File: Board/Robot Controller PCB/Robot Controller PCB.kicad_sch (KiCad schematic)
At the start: 1 part

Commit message: Started shematic
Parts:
- added R, R?: 10k, symbol Device:R_Small_US
- added R?: 20k, symbol Device:R_Small_US
- added R?: 80k, symbol Device:R_Small_US
- added R?: 40k, symbol Device:R_Small_US
- added SW? (x2): SW_DPST_x2, symbol Switch:SW_DPST_x2
- added SW?: SW_DIP_x04, symbol Switch:SW_DIP_x04
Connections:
- net +5V: now reaches U?.21 (VCC)
- net +5V: now also SW?.1, SW?.2, SW?.3, SW?.4
- net GND: now reaches U?.23 (GND)
- net GND: now also U?.3 (GND), U?.4 (GND), R?.2, SW?.1 (A), SW?.3 (A)
- net at U?.5 (D2): now also SW?.2 (B)
- net at U?.6 (~D3): now also SW?.4 (B)
- net at U?.7 (D4/A6): now also R.1, R?.1, R?.2, R?.2, R?.2
- new net: R?.1, SW?.7
- new net: R?.1, SW?.5
- new net: R.2, SW?.8
- new net: R?.1, SW?.6
- no-connect marks 0 -> 5

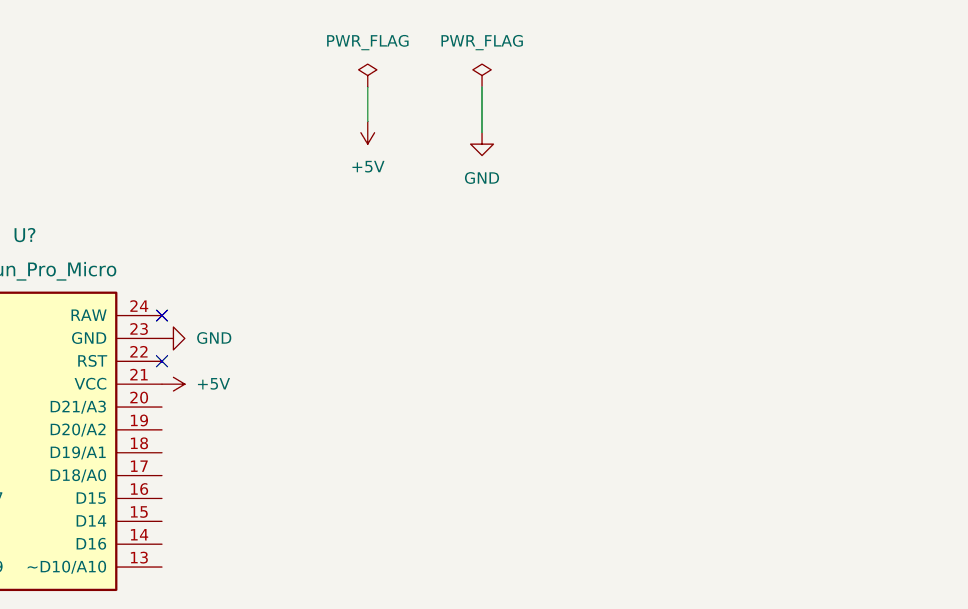
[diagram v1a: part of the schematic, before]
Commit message: Added sliders
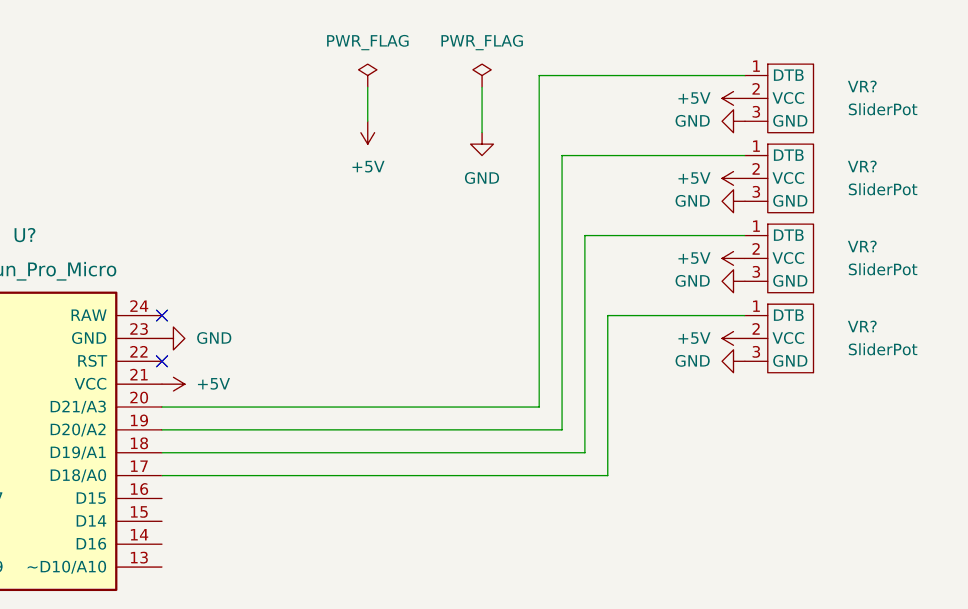
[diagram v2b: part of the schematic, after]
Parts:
- added VR? (x4): SliderPot, RobotController:SliderPot, symbol RobotController:SliderPot
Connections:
- net +5V: now also VR?.2 (VCC), VR?.2 (VCC), VR?.2 (VCC), VR?.2 (VCC)
- net GND: now also VR?.3 (GND), VR?.3 (GND), VR?.3 (GND), VR?.3 (GND)
- net at U?.17 (D18/A0): now also VR?.1 (DTB)
- net at U?.18 (D19/A1): now also VR?.1 (DTB)
- net at U?.19 (D20/A2): now also VR?.1 (DTB)
- net at U?.20 (D21/A3): now also VR?.1 (DTB)

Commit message: Started pcb, finished schematic
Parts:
- removed SW? (x2): SW_DPST_x2, symbol Switch:SW_DPST_x2
- added SW2, SW3: SW_Push, Connector_PinHeader_2.54mm:PinHeader_1x02_P2.54mm_Vertical, symbol Switch:SW_Push
- added sw_led1, sw_led2, sw_led3, sw_led4: ArcadeButton, RobotController:ArcadeButton, symbol RobotController:ArcadeButton
- R1: renamed from R; footprint (none) -> Resistor_THT:R_Axial_DIN0207_L6.3mm_D2.5mm_P10.16mm_Horizontal
- R2, R3, R4, R5: renamed from R?; footprint (none) -> Resistor_THT:R_Axial_DIN0207_L6.3mm_D2.5mm_P10.16mm_Horizontal
- SW1: renamed from SW?; footprint (none) -> Package_DIP:DIP-8_W7.62mm
- gave numbers to parts that had none: 5
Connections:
- net GND: now also SW2.1, SW3.1, sw_led1.3 (GND), sw_led2.3 (GND), sw_led3.3 (GND), sw_led4.3 (GND)
- net at U1.6 (~D3): now also SW3.2
- net at U1.10 (D7): now also sw_led3.2 (LED)
- net at U1.11 (D8/A8): now also sw_led2.2 (LED)
- net at U1.12 (~D9/A9): now also sw_led1.2 (LED)
- net at U1.13 (~D10/A10): now also sw_led1.1 (Button)
- net at U1.14 (D16): now also sw_led2.1 (Button)
- net at U1.15 (D14): now also sw_led3.1 (Button)
- net at U1.16 (D15): now also sw_led4.1 (Button)
- net at U1.5 (D2): now also SW2.2
- net at U1.9 (~D6/A7): now also sw_led4.2 (LED)

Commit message: Done....for now
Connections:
- net at U1.10 (D7): now also sw_led2.2 (LED); no longer sw_led3.2 (LED)
- net at U1.11 (D8/A8): now also sw_led1.1 (Button); no longer sw_led2.2 (LED)
- net at U1.13 (~D10/A10): now also sw_led3.2 (LED); no longer sw_led1.1 (Button)
- net at U1.14 (D16): now also sw_led3.1 (Button); no longer sw_led2.1 (Button)
- net at U1.15 (D14): now also sw_led4.2 (LED); no longer sw_led3.1 (Button)
- net at U1.9 (~D6/A7): now also sw_led2.1 (Button); no longer sw_led4.2 (LED)
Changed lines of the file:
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@@
   (no_connect (at 110.49 66.04))
   (no_connect (at 110.49 60.96))
-  (wire (pts (xy 77.47 88.9) (xy 80.01 88.9))
-    (stroke (width 0) (type default) (color 0 0 0 0))
-  )
-  (wire (pts (xy 118.11 86.36) (xy 110.49 86.36))
-    (stroke (width 0) (type default) (color 0 0 0 0))
-  )
   (wire (pts (xy 160.02 60.96) (xy 160.02 78.74))
     (stroke (width 0) (type default) (color 0 0 0 0))
@@
     (stroke (width 0) (type default) (color 0 0 0 0))
   )
-  (wire (pts (xy 69.85 81.28) (xy 80.01 81.28))
+  (wire (pts (xy 93.98 116.84) (xy 93.98 97.79))
     (stroke (width 0) (type default) (color 0 0 0 0))
   )
   (wire (pts (xy 69.85 41.91) (xy 69.85 71.12))
-    (stroke (width 0) (type default) (color 0 0 0 0))
-  )
-  (wire (pts (xy 72.39 83.82) (xy 80.01 83.82))
-    (stroke (width 0) (type default) (color 0 0 0 0))
-  )
-  (wire (pts (xy 113.03 100.33) (xy 113.03 88.9))
     (stroke (width 0) (type default) (color 0 0 0 0))
   )
@@
     (stroke (width 0) (type default) (color 0 0 0 0))
   )
-  (wire (pts (xy 96.52 154.94) (xy 123.19 154.94))
+  (wire (pts (xy 120.65 153.67) (xy 120.65 86.36))
+    (stroke (width 0) (type default) (color 0 0 0 0))
+  )
+  (wire (pts (xy 77.47 88.9) (xy 80.01 88.9))
     (stroke (width 0) (type default) (color 0 0 0 0))
   )
@@
     (stroke (width 0) (type default) (color 0 0 0 0))
   )
+  (wire (pts (xy 95.25 168.91) (xy 123.19 168.91))
+    (stroke (width 0) (type default) (color 0 0 0 0))
+  )
+  (wire (pts (xy 120.65 86.36) (xy 110.49 86.36))
+    (stroke (width 0) (type default) (color 0 0 0 0))
+  )
   (wire (pts (xy 175.26 52.07) (xy 157.48 52.07))
+    (stroke (width 0) (type default) (color 0 0 0 0))
+  )
+  (wire (pts (xy 123.19 83.82) (xy 110.49 83.82))
     (stroke (width 0) (type default) (color 0 0 0 0))
   )
@@
     (stroke (width 0) (type default) (color 0 0 0 0))
   )
-  (wire (pts (xy 72.39 149.86) (xy 72.39 83.82))
+  (wire (pts (xy 96.52 135.89) (xy 96.52 128.27))
     (stroke (width 0) (type default) (color 0 0 0 0))
   )
-  (wire (pts (xy 96.52 100.33) (xy 113.03 100.33))
+  (wire (pts (xy 93.98 151.13) (xy 118.11 151.13))
     (stroke (width 0) (type default) (color 0 0 0 0))
   )
   (wire (pts (xy 175.26 60.96) (xy 160.02 60.96))
-    (stroke (width 0) (type default) (color 0 0 0 0))
-  )
-  (wire (pts (xy 93.98 149.86) (xy 72.39 149.86))
     (stroke (width 0) (type default) (color 0 0 0 0))
   )
@@
     (stroke (width 0) (type default) (color 0 0 0 0))
   )
-  (wire (pts (xy 93.98 135.89) (xy 93.98 130.81))
-    (stroke (width 0) (type default) (color 0 0 0 0))
-  )
-  (wire (pts (xy 76.2 86.36) (xy 80.01 86.36))
-    (stroke (width 0) (type default) (color 0 0 0 0))
-  )
-  (wire (pts (xy 113.03 88.9) (xy 110.49 88.9))
+  (wire (pts (xy 72.39 99.06) (xy 72.39 81.28))
     (stroke (width 0) (type default) (color 0 0 0 0))
   )
@@
     (stroke (width 0) (type default) (color 0 0 0 0))
   )
+  (wire (pts (xy 93.98 132.08) (xy 69.85 132.08))
+    (stroke (width 0) (type default) (color 0 0 0 0))
+  )
   (wire (pts (xy 125.73 81.28) (xy 110.49 81.28))
     (stroke (width 0) (type default) (color 0 0 0 0))
@@
     (stroke (width 0) (type default) (color 0 0 0 0))
   )
-  (wire (pts (xy 157.48 52.07) (xy 157.48 76.2))
+  (wire (pts (xy 74.93 95.25) (xy 74.93 86.36))
     (stroke (width 0) (type default) (color 0 0 0 0))
   )
-  (wire (pts (xy 77.47 100.33) (xy 77.47 88.9))
+  (wire (pts (xy 157.48 52.07) (xy 157.48 76.2))
     (stroke (width 0) (type default) (color 0 0 0 0))
   )
@@
     (stroke (width 0) (type default) (color 0 0 0 0))
   )
-  (wire (pts (xy 93.98 116.84) (xy 93.98 100.33))
+  (wire (pts (xy 95.25 171.45) (xy 95.25 168.91))
     (stroke (width 0) (type default) (color 0 0 0 0))
   )
-  (wire (pts (xy 96.52 130.81) (xy 118.11 130.81))
+  (wire (pts (xy 118.11 88.9) (xy 110.49 88.9))
     (stroke (width 0) (type default) (color 0 0 0 0))
   )
@@
     (stroke (width 0) (type default) (color 0 0 0 0))
   )
-  (wire (pts (xy 93.98 100.33) (xy 77.47 100.33))
-    (stroke (width 0) (type default) (color 0 0 0 0))
-  )
-  (wire (pts (xy 96.52 135.89) (xy 96.52 130.81))
+  (wire (pts (xy 96.52 153.67) (xy 120.65 153.67))
     (stroke (width 0) (type default) (color 0 0 0 0))
   )
@@
     (stroke (width 0) (type default) (color 0 0 0 0))
   )
-  (wire (pts (xy 24.13 45.72) (xy 24.13 48.26))
+  (wire (pts (xy 93.98 97.79) (xy 77.47 97.79))
     (stroke (width 0) (type default) (color 0 0 0 0))
   )
-  (wire (pts (xy 76.2 130.81) (xy 76.2 86.36))
+  (wire (pts (xy 72.39 81.28) (xy 80.01 81.28))
+    (stroke (width 0) (type default) (color 0 0 0 0))
+  )
+  (wire (pts (xy 69.85 83.82) (xy 80.01 83.82))
+    (stroke (width 0) (type default) (color 0 0 0 0))
+  )
+  (wire (pts (xy 96.52 95.25) (xy 74.93 95.25))
+    (stroke (width 0) (type default) (color 0 0 0 0))
+  )
+  (wire (pts (xy 74.93 86.36) (xy 80.01 86.36))
+    (stroke (width 0) (type default) (color 0 0 0 0))
+  )
+  (wire (pts (xy 24.13 45.72) (xy 24.13 48.26))
     (stroke (width 0) (type default) (color 0 0 0 0))
   )
@@
     (stroke (width 0) (type default) (color 0 0 0 0))
   )
-  (wire (pts (xy 123.19 83.82) (xy 110.49 83.82))
+  (wire (pts (xy 87.63 128.27) (xy 87.63 99.06))
     (stroke (width 0) (type default) (color 0 0 0 0))
   )
-  (wire (pts (xy 123.19 154.94) (xy 123.19 83.82))
+  (wire (pts (xy 118.11 151.13) (xy 118.11 88.9))
     (stroke (width 0) (type default) (color 0 0 0 0))
   )
-  (wire (pts (xy 93.98 154.94) (xy 93.98 149.86))
+  (wire (pts (xy 87.63 99.06) (xy 72.39 99.06))
     (stroke (width 0) (type default) (color 0 0 0 0))
   )
@@
     (stroke (width 0) (type default) (color 0 0 0 0))
   )
-  (wire (pts (xy 118.11 130.81) (xy 118.11 86.36))
-    (stroke (width 0) (type default) (color 0 0 0 0))
-  )
-  (wire (pts (xy 95.25 166.37) (xy 69.85 166.37))
+  (wire (pts (xy 96.52 128.27) (xy 87.63 128.27))
     (stroke (width 0) (type default) (color 0 0 0 0))
   )
@@
     (stroke (width 0) (type default) (color 0 0 0 0))
   )
-  (wire (pts (xy 69.85 166.37) (xy 69.85 81.28))
-    (stroke (width 0) (type default) (color 0 0 0 0))
-  )
   (wire (pts (xy 154.94 43.18) (xy 154.94 73.66))
     (stroke (width 0) (type default) (color 0 0 0 0))
@@
     (stroke (width 0) (type default) (color 0 0 0 0))
   )
-  (wire (pts (xy 95.25 171.45) (xy 95.25 166.37))
+  (wire (pts (xy 96.52 116.84) (xy 96.52 95.25))
     (stroke (width 0) (type default) (color 0 0 0 0))
   )
@@
     (stroke (width 0) (type default) (color 0 0 0 0))
   )
-  (wire (pts (xy 96.52 116.84) (xy 96.52 100.33))
+  (wire (pts (xy 77.47 97.79) (xy 77.47 88.9))
+    (stroke (width 0) (type default) (color 0 0 0 0))
+  )
+  (wire (pts (xy 96.52 154.94) (xy 96.52 153.67))
     (stroke (width 0) (type default) (color 0 0 0 0))
   )
@@
     (stroke (width 0) (type default) (color 0 0 0 0))
   )
-  (wire (pts (xy 93.98 130.81) (xy 76.2 130.81))
+  (wire (pts (xy 93.98 154.94) (xy 93.98 151.13))
     (stroke (width 0) (type default) (color 0 0 0 0))
   )
@@
     (stroke (width 0) (type default) (color 0 0 0 0))
   )
+  (wire (pts (xy 123.19 168.91) (xy 123.19 83.82))
+    (stroke (width 0) (type default) (color 0 0 0 0))
+  )
+  (wire (pts (xy 69.85 132.08) (xy 69.85 83.82))
+    (stroke (width 0) (type default) (color 0 0 0 0))
+  )
+  (wire (pts (xy 93.98 135.89) (xy 93.98 132.08))
+    (stroke (width 0) (type default) (color 0 0 0 0))
+  )
